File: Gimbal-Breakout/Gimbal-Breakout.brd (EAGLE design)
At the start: 31.8 x 54.4 mm, 4 parts

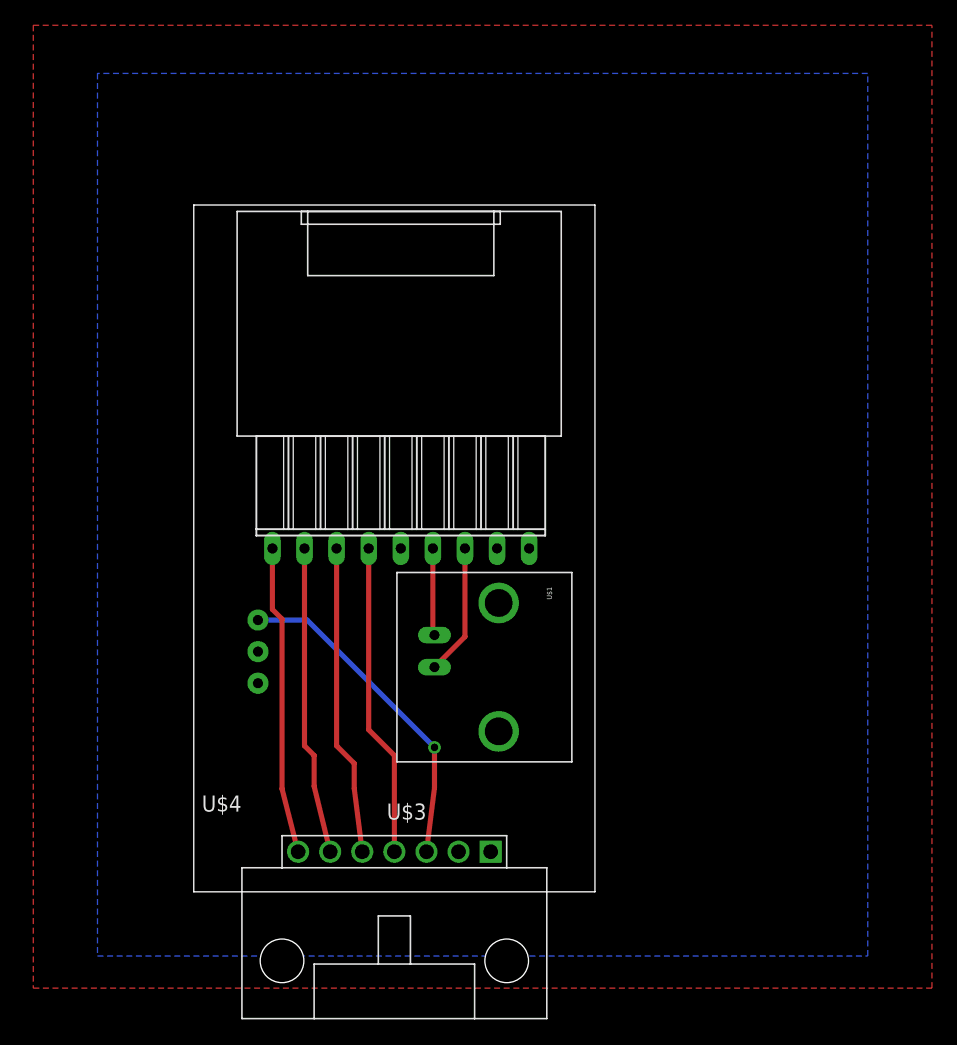
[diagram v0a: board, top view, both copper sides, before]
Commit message: finished gimbal breakout
added mounting holes
labeled board
fixed traces
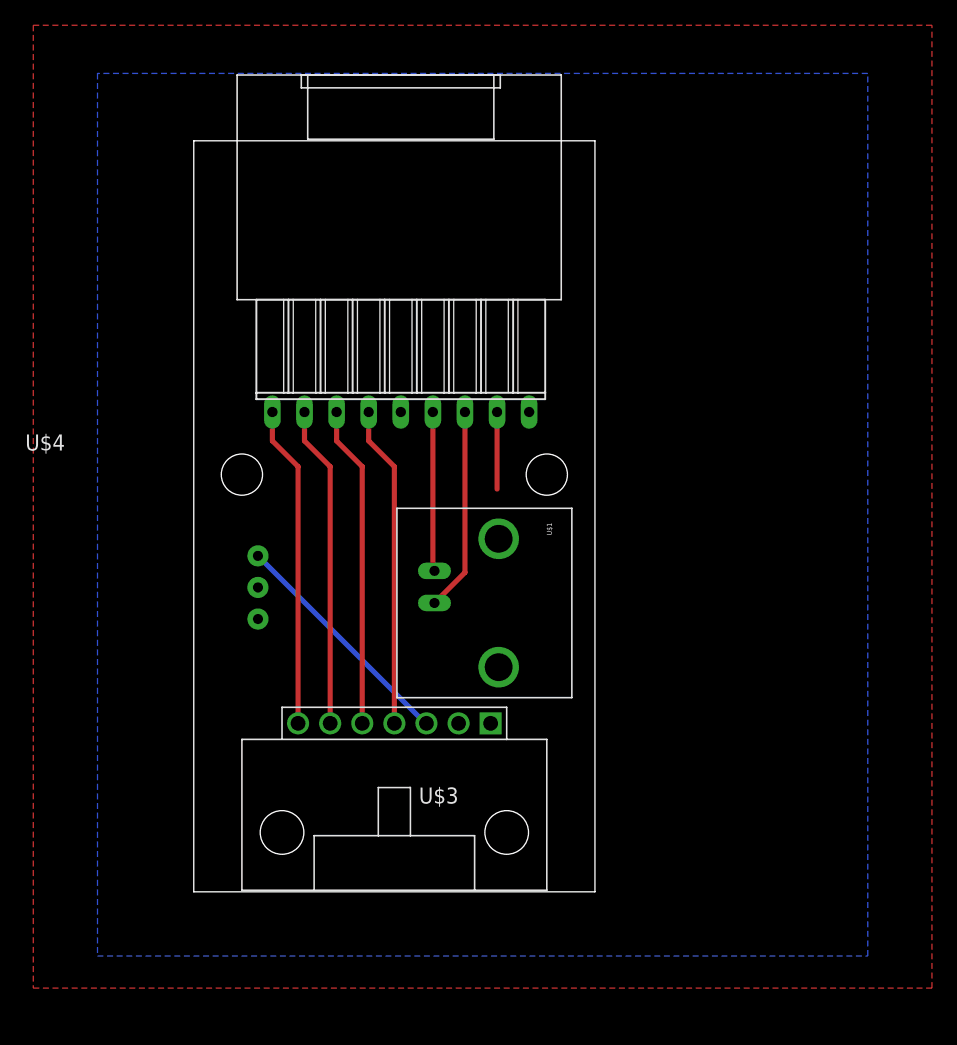
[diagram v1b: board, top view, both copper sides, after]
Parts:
- added H1, H2: MOUNTING_HOLE#4, MRDT-Hardware:#4_SCREW
- added LOGO1: MRDT_LOGO, MRDT-Hardware:MRDT_LOGO
- moved U$4 10.8 mm to (3.17, 36.2)
- moved U$3 10.2 mm to (15.9, 13.3)
- moved DYNA2 5.08 mm to (5.08, 21.6)
- moved U$1 5.08 mm to (19.1, 22.9)
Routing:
- net DYNA_DATA: track 26.4 -> 18.8 mm, vias 1 -> 0
- net CAM_VIDEO_GND: track 6.91 -> 12.6 mm
- net CAM_VIDEO: track 10.4 -> 16.1 mm
- net +12V: track 0.38 -> 6.10 mm
- net CAM_PWM2: track 24.5 -> 25.5 mm
- net CAM_PWM3: track 24.5 -> 25.5 mm
- net CAM_PWM1: track 24.6 -> 25.5 mm
- net CAM_PWM0: track 24.8 -> 25.5 mm
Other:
- board size 31.8 x 54.4 mm -> 31.8 x 59.4 mm
- board text added: "Missouri S&T Mars Rover Design Team Camera Gimbal Breakout"
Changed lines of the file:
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@@
 <layer number="45" name="Holes" color="7" fill="1" visible="no" active="yes"/>
 <layer number="46" name="Milling" color="3" fill="1" visible="no" active="yes"/>
-<layer number="47" name="Measures" color="7" fill="1" visible="yes" active="yes"/>
+<layer number="47" name="Measures" color="7" fill="1" visible="no" active="yes"/>
 <layer number="48" name="Document" color="7" fill="1" visible="yes" active="yes"/>
 <layer number="49" name="Reference" color="7" fill="1" visible="yes" active="yes"/>
@@
 <plain>
 <wire x1="0" y1="0" x2="31.75" y2="0" width="0" layer="20"/>
-<wire x1="31.75" y1="0" x2="31.75" y2="54.356" width="0" layer="20"/>
-<wire x1="31.75" y1="54.356" x2="0" y2="54.356" width="0" layer="20"/>
-<wire x1="0" y1="54.356" x2="0" y2="0" width="0" layer="20"/>
+<wire x1="31.75" y1="0" x2="31.75" y2="59.436" width="0" layer="20"/>
+<wire x1="31.75" y1="59.436" x2="0" y2="59.436" width="0" layer="20"/>
+<wire x1="0" y1="59.436" x2="0" y2="0" width="0" layer="20"/>
 <dimension x1="0" y1="0" x2="31.75" y2="0" x3="15.875" y3="-19.558" textsize="1.778" layer="47" unit="inch" precision="6" visible="yes"/>
 <dimension x1="31.75" y1="0" x2="31.75" y2="54.356" x3="71.374" y3="27.178" textsize="1.778" layer="47" unit="inch" precision="6" visible="yes"/>
+<text x="15.875" y="52.705" size="1.27" layer="22" rot="MR180" align="center">Missouri S&amp;T
+Mars Rover Design Team
+Camera Gimbal Breakout</text>
 </plain>
 <attributes>
@@
 </autorouter>
 <elements>
-<element name="DYNA2" library="MRDT-2015-Arm" package="MLX-SPOX5268-3PIN" value="DYNAMIXEL-1X03HORIZ" x="5.08" y="16.51" rot="R90">
-<attribute name="MFR" value="Molex" x="53.34" y="48.26" size="1.778" layer="27" rot="R90" display="off"/>
-<attribute name="MFR_PN" value="0022057035" x="53.34" y="48.26" size="1.778" layer="27" rot="R90" display="off"/>
-<attribute name="ORIENT" value="Horiz" x="53.34" y="48.26" size="1.778" layer="27" rot="R90" display="off"/>
+<element name="DYNA2" library="MRDT-2015-Arm" package="MLX-SPOX5268-3PIN" value="DYNAMIXEL-1X03HORIZ" x="5.08" y="21.59" rot="R90">
+<attribute name="MFR" value="Molex" x="53.34" y="53.34" size="1.778" layer="27" rot="R90" display="off"/>
+<attribute name="MFR_PN" value="0022057035" x="53.34" y="53.34" size="1.778" layer="27" rot="R90" display="off"/>
+<attribute name="ORIENT" value="Horiz" x="53.34" y="53.34" size="1.778" layer="27" rot="R90" display="off"/>
 </element>
-<element name="U$1" library="SparkFun-Connectors" package="BNC" value="BNCPTH" x="19.05" y="17.78" rot="R270"/>
-<element name="U$3" library="MRDT-Connectors" package="MOLEX-70551-0006" value="SL07-HORIZ" x="15.875" y="3.175" rot="R180"/>
-<element name="U$4" library="MRDT-2015-General" package="CAM_CONNECTOR" value="CAMERA_BREAKOUT" x="3.175" y="25.4"/>
+<element name="U$1" library="SparkFun-Connectors" package="BNC" value="BNCPTH" x="19.05" y="22.86" smashed="yes" rot="R270">
+<attribute name="NAME" x="27.94" y="29.21" size="0.4064" layer="25" rot="R270"/>
+<attribute name="VALUE" x="26.67" y="29.21" size="0.4064" layer="27" rot="SR270"/>
+</element>
+<element name="U$3" library="MRDT-Connectors" package="MOLEX-70551-0006" value="SL07-HORIZ" x="15.875" y="13.335" smashed="yes" rot="R180">
+<attribute name="NAME" x="20.955" y="8.255" size="1.27" layer="25" rot="R180"/>
+</element>
+<element name="U$4" library="MRDT-2015-General" package="CAM_CONNECTOR" value="CAMERA_BREAKOUT" x="3.175" y="36.195" smashed="yes">
+<attribute name="NAME" x="-13.335" y="34.925" size="1.27" layer="25" ratio="10"/>
+<attribute name="VALUE" x="-21.717" y="30.607" size="1.27" layer="27" ratio="10" rot="R90"/>
+</element>
+<element name="H1" library="MRDT-Hardware" package="#4_SCREW" value="MOUNTING_HOLE#4" x="3.81" y="33.02"/>
+<element name="H2" library="MRDT-Hardware" package="#4_SCREW" value="MOUNTING_HOLE#4" x="27.94" y="33.02"/>
+<element name="LOGO1" library="MRDT-Hardware" package="MRDT_LOGO" value="MRDT_LOGO" x="19.685" y="38.735" rot="MR0"/>
 </elements>
 <signals>
@@
 <contactref element="U$4" pad="8"/>
 <contactref element="U$3" pad="2"/>
-<wire x1="24.003" y1="27.178" x2="24.003" y2="26.797" width="0.4064" layer="1"/>
+<wire x1="24.003" y1="37.973" x2="24.003" y2="31.877" width="0.4064" layer="1"/>
 <polygon width="0.4064" layer="1">
 <vertex x="-12.7" y="-7.62"/>
@@
 <contactref element="DYNA2" pad="DATA"/>
 <contactref element="U$3" pad="3"/>
-<wire x1="5.08" y1="21.51" x2="8.97" y2="21.51" width="0.4064" layer="16"/>
-<wire x1="8.97" y1="21.51" x2="19.05" y2="11.43" width="0.4064" layer="16"/>
-<via x="19.05" y="11.43" extent="1-16" drill="0.6"/>
-<wire x1="19.05" y1="11.43" x2="19.05" y2="8.2296" width="0.4064" layer="1"/>
-<wire x1="19.05" y1="8.2296" x2="18.415" y2="3.175" width="0.4064" layer="1"/>
+<wire x1="18.415" y1="13.335" x2="18.335" y2="13.335" width="0.4064" layer="16"/>
+<wire x1="18.335" y1="13.335" x2="5.08" y2="26.59" width="0.4064" layer="16"/>
 </signal>
 <signal name="CAM_VIDEO">
 <contactref element="U$1" pad="S"/>
 <contactref element="U$4" pad="7"/>
-<wire x1="21.463" y1="27.178" x2="21.463" y2="20.193" width="0.4064" layer="1"/>
-<wire x1="21.463" y1="20.193" x2="19.05" y2="17.78" width="0.4064" layer="1"/>
+<wire x1="21.463" y1="37.973" x2="21.463" y2="25.273" width="0.4064" layer="1"/>
+<wire x1="21.463" y1="25.273" x2="19.05" y2="22.86" width="0.4064" layer="1"/>
 </signal>
 <signal name="CAM_VIDEO_GND">
 <contactref element="U$1" pad="GND"/>
 <contactref element="U$4" pad="6"/>
-<wire x1="18.923" y1="27.178" x2="18.923" y2="20.447" width="0.4064" layer="1"/>
-<wire x1="18.923" y1="20.447" x2="19.05" y2="20.32" width="0.4064" layer="1"/>
+<wire x1="18.923" y1="37.973" x2="18.923" y2="25.527" width="0.4064" layer="1"/>
+<wire x1="18.923" y1="25.527" x2="19.05" y2="25.4" width="0.4064" layer="1"/>
 </signal>
 <signal name="CAM_PWM3">
 <contactref element="U$4" pad="1"/>
 <contactref element="U$3" pad="7"/>
-<wire x1="6.223" y1="27.178" x2="6.223" y2="22.352" width="0.4064" layer="1"/>
-<wire x1="6.223" y1="22.352" x2="6.985" y2="21.59" width="0.4064" layer="1"/>
-<wire x1="6.985" y1="21.59" x2="6.985" y2="8.1534" width="0.4064" layer="1"/>
-<wire x1="6.985" y1="8.1534" x2="8.255" y2="3.175" width="0.4064" layer="1"/>
+<wire x1="8.255" y1="13.335" x2="8.255" y2="33.655" width="0.4064" layer="1"/>
+<wire x1="6.223" y1="35.687" x2="6.223" y2="37.973" width="0.4064" layer="1"/>
+<wire x1="8.255" y1="33.655" x2="6.223" y2="35.687" width="0.4064" layer="1"/>
 </signal>
 <signal name="CAM_PWM2">
 <contactref element="U$4" pad="2"/>
 <contactref element="U$3" pad="6"/>
-<wire x1="8.763" y1="27.178" x2="8.763" y2="11.557" width="0.4064" layer="1"/>
-<wire x1="8.763" y1="11.557" x2="9.525" y2="10.795" width="0.4064" layer="1"/>
-<wire x1="9.525" y1="10.795" x2="9.525" y2="8.3566" width="0.4064" layer="1"/>
-<wire x1="9.525" y1="8.3566" x2="10.795" y2="3.175" width="0.4064" layer="1"/>
+<wire x1="10.795" y1="13.335" x2="10.795" y2="33.655" width="0.4064" layer="1"/>
+<wire x1="8.763" y1="35.687" x2="8.763" y2="37.973" width="0.4064" layer="1"/>
+<wire x1="10.795" y1="33.655" x2="8.763" y2="35.687" width="0.4064" layer="1"/>
 </signal>
 <signal name="CAM_PWM1">
 <contactref element="U$4" pad="3"/>
 <contactref element="U$3" pad="5"/>
-<wire x1="11.303" y1="27.178" x2="11.303" y2="11.557" width="0.4064" layer="1"/>
-<wire x1="11.303" y1="11.557" x2="12.7" y2="10.16" width="0.4064" layer="1"/>
-<wire x1="12.7" y1="10.16" x2="12.7" y2="8.1788" width="0.4064" layer="1"/>
-<wire x1="12.7" y1="8.1788" x2="13.335" y2="3.175" width="0.4064" layer="1"/>
+<wire x1="13.335" y1="13.335" x2="13.335" y2="33.655" width="0.4064" layer="1"/>
+<wire x1="11.303" y1="35.687" x2="11.303" y2="37.973" width="0.4064" layer="1"/>
+<wire x1="13.335" y1="33.655" x2="11.303" y2="35.687" width="0.4064" layer="1"/>
 </signal>
 <signal name="CAM_PWM0">
 <contactref element="U$4" pad="4"/>
 <contactref element="U$3" pad="4"/>
-<wire x1="13.843" y1="27.178" x2="13.843" y2="12.827" width="0.4064" layer="1"/>
-<wire x1="13.843" y1="12.827" x2="15.875" y2="10.795" width="0.4064" layer="1"/>
-<wire x1="15.875" y1="10.795" x2="15.875" y2="3.175" width="0.4064" layer="1"/>
+<wire x1="15.875" y1="13.335" x2="15.875" y2="33.655" width="0.4064" layer="1"/>
+<wire x1="13.843" y1="35.687" x2="13.843" y2="37.973" width="0.4064" layer="1"/>
+<wire x1="15.875" y1="33.655" x2="13.843" y2="35.687" width="0.4064" layer="1"/>
 </signal>
 </signals>
 </board>
 </drawing>
+<compatibility>
+<note version="6.3" minversion="6.2.2" severity="warning">
+Since Version 6.2.2 text objects can contain more than one line,
+which will not be processed correctly with this version.
+</note>
+</compatibility>
 </eagle>
